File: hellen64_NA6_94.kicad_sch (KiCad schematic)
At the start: 208 parts, among them J1 USB_B_Mini, J11 Conn_01x01, J13 Conn_01x01, J14 Conn_01x01, J15 Conn_01x01, J16 Conn_01x01, J17 Conn_01x01, J19 Conn_01x01, J2 Conn_01x05_Male, J20 Conn_01x01, J21 Conn_01x01, J22 Conn_01x01, J24 Conn_01x01, J25 AudioJack3_SwitchTR, J27 Conn_01x06, J4 Conn_02x12_Odd_Even, J5 USB_B, M1 Module-input-0.1, M10 Module-power12-0.2, M11 Module-power5-0.2, M12 Module-wbo-0.3, M13 Module-can-0.1, M2 Module-ign8-0.2, M3 Module-mcu144-0.6, M4 Module-sd-0.1, M5 Module-output-0.3, M6 Module-dinput4-0.1, M7 Module-stlink-0.1, M8 Module-can-0.1, M9 Module-knock-0.1, P1 Pad, P10 Pad, P11 Pad, P12 Pad, P13 Pad, P14 Pad, P15 Pad, P16 Pad, P17 Pad, P18 Pad, P19 Pad, P2 178780-1, P20 Pad, P21 Pad, P22 Pad, P23 Pad, P24 Pad, P25 Pad, P26 Pad, P27 Pad, P28 Pad, P29 Pad, P3 Pad, P30 Pad, P31 Pad, P32 Pad, P33 Pad, P34 Pad, P35 Pad, P36 Pad, P37 Pad, P38 Pad, P39 Pad, P4 Pad, P40 Pad, P41 Pad, P42 Pad, P43 Pad, P44 Pad, P45 Pad, P46 Pad, P5 Pad, P6 Pad, P7 Pad, P8 Pad, P9 Pad, U1 LIS2DW12TR, U2 MPX4_MAP, U3 MCP6002-xSN, U4 LPS25HB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

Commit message: https://github.com/rusefi/hellenNA6_issues/issues/28
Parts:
- added U7: MPXH6400A, hellen-one-common:MPXH6400A-SSOP8, symbol MPX-4_MAP:MPX4_MAP
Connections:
- net +5VA: now also U7.2 (Vs)
- net GND: now also U7.3 (GND)
- net IN_MAP3: now also U7.4 (Vout)
- no-connect marks 59 -> 64
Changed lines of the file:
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@@
   (title_block
     (title "hellen64 NA6 94")
-    (date "2022-06-23")
+    (date "2022-06-24")
     (rev "С")
     (company "rusEFI")
@@
   (junction (at 26.67 392.43) (diameter 1.016) (color 0 0 0 0)
   )
+  (junction (at 265.43 228.6) (diameter 0) (color 0 0 0 0)
+  )
   (junction (at 62.23 43.18) (diameter 1.016) (color 0 0 0 0)
   )
@@
   (no_connect (at 365.76 165.1))
   (no_connect (at 518.16 377.19))
+  (no_connect (at 251.46 256.54))
   (no_connect (at 36.83 326.39))
   (no_connect (at 455.93 109.22))
@@
   (no_connect (at 307.34 50.8))
   (no_connect (at 36.83 311.15))
+  (no_connect (at 226.06 251.46))
   (no_connect (at 26.67 311.15))
   (no_connect (at 251.46 236.22))
@@
   (no_connect (at 69.85 38.1))
   (no_connect (at 307.34 53.34))
+  (no_connect (at 226.06 256.54))
   (no_connect (at 132.08 176.53))
+  (no_connect (at 226.06 254))
   (no_connect (at 415.29 114.3))
   (no_connect (at 307.34 45.72))
+  (no_connect (at 226.06 248.92))
   (no_connect (at 473.71 375.92))
   (no_connect (at 307.34 55.88))
@@
     (stroke (width 0) (type solid) (color 0 0 0 0))
   )
-  (wire (pts (xy 229.87 25.4) (xy 229.87 265.43))
+  (wire (pts (xy 229.87 25.4) (xy 229.87 243.84))
     (stroke (width 0) (type default) (color 0 0 0 0))
   )
@@
     (stroke (width 0) (type solid) (color 0 0 0 0))
   )
-  (wire (pts (xy 251.46 228.6) (xy 270.51 228.6))
+  (wire (pts (xy 251.46 228.6) (xy 265.43 228.6))
     (stroke (width 0) (type solid) (color 0 0 0 0))
   )
@@
     (stroke (width 0) (type solid) (color 0 0 0 0))
   )
+  (wire (pts (xy 265.43 228.6) (xy 270.51 228.6))
+    (stroke (width 0) (type solid) (color 0 0 0 0))
+  )
   (wire (pts (xy 111.76 233.68) (xy 220.98 233.68))
     (stroke (width 0) (type default) (color 0 0 0 0))
@@
     (stroke (width 0) (type solid) (color 0 0 0 0))
   )
+  (wire (pts (xy 259.08 254) (xy 251.46 254))
+    (stroke (width 0) (type default) (color 0 0 0 0))
+  )
   (bus (pts (xy 273.05 247.65) (xy 273.05 250.19))
     (stroke (width 0.3048) (type solid) (color 255 0 255 1))
@@
     (stroke (width 0) (type solid) (color 0 0 0 0))
   )
+  (wire (pts (xy 265.43 228.6) (xy 265.43 248.92))
+    (stroke (width 0) (type default) (color 0 0 0 0))
+  )
   (wire (pts (xy 39.37 353.06) (xy 36.83 353.06))
     (stroke (width 0) (type solid) (color 0 0 0 0))
@@
     (stroke (width 0) (type solid) (color 0 0 0 0))
   )
+  (wire (pts (xy 251.46 248.92) (xy 265.43 248.92))
+    (stroke (width 0) (type solid) (color 0 0 0 0))
+  )
   (wire (pts (xy 426.72 311.15) (xy 431.8 311.15))
     (stroke (width 0) (type default) (color 0 0 0 0))
@@
     (stroke (width 0) (type solid) (color 0 0 0 0))
   )
+  (wire (pts (xy 224.79 265.43) (xy 224.79 243.84))
+    (stroke (width 0) (type default) (color 0 0 0 0))
+  )
   (wire (pts (xy 46.99 358.14) (xy 59.69 358.14))
     (stroke (width 0) (type solid) (color 0 0 0 0))
@@
     (stroke (width 0) (type solid) (color 0 0 0 0))
   )
-  (wire (pts (xy 205.74 265.43) (xy 229.87 265.43))
+  (wire (pts (xy 205.74 265.43) (xy 224.79 265.43))
     (stroke (width 0) (type solid) (color 0 0 0 0))
   )
@@
     (stroke (width 0.3048) (type solid) (color 255 0 0 1))
   )
+  (wire (pts (xy 224.79 243.84) (xy 229.87 243.84))
+    (stroke (width 0) (type default) (color 0 0 0 0))
+  )
   (wire (pts (xy 271.78 212.09) (xy 309.88 212.09))
     (stroke (width 0) (type solid) (color 0 0 0 0))
@@
     (effects (font (size 1.27 1.27)) (justify right bottom))
   )
+  (label "IN_MAP3" (at 261.62 248.92 180)
+    (effects (font (size 1.27 1.27)) (justify right bottom))
+  )
   (label "IN_RES1" (at 297.18 240.03 0)
     (effects (font (size 1.27 1.27)) (justify left bottom))
@@
     (pin "1")
   )
+  (symbol (lib_id "power:+5VA") (at 259.08 254 270) (mirror x) (unit 1)
+    (in_bom yes) (on_board yes)
+    (property "Reference" "#PWR097" (id 0) (at 255.27 254 0)
+      (effects (font (size 1.27 1.27)) hide)
+    )
+    (property "Value" "+5VA" (id 1) (at 262.1344 253.6317 0))
+    (property "Footprint" "" (id 2) (at 259.08 254 0)
+      (effects (font (size 1.27 1.27)) hide)
+    )
+    (property "Datasheet" "" (id 3) (at 259.08 254 0)
+      (effects (font (size 1.27 1.27)) hide)
+    )
+    (pin "1")
+  )
   (symbol (lib_id "Device:C") (at 232.41 349.25 0) (mirror x) (unit 1)
     (in_bom yes) (on_board yes)
@@
     (pin "8")
   )
+  (symbol (lib_id "power:GND") (at 251.46 251.46 90) (mirror x) (unit 1)
+    (in_bom yes) (on_board yes)
+    (property "Reference" "#PWR055" (id 0) (at 257.81 251.46 0)
+      (effects (font (size 1.27 1.27)) hide)
+    )
+    (property "Value" "GND" (id 1) (at 255.905 251.46 90))
+    (property "Footprint" "" (id 2) (at 251.46 251.46 0)
+      (effects (font (size 1.27 1.27)) hide)
+    )
+    (property "Datasheet" "" (id 3) (at 251.46 251.46 0)
+      (effects (font (size 1.27 1.27)) hide)
+    )
+    (pin "1")
+  )
   (symbol (lib_id "power:GND") (at 193.04 328.93 0) (unit 1)
     (in_bom yes) (on_board yes)
@@
     (pin "1")
   )
+  (symbol (lib_name "MPX4_MAP_1") (lib_id "MPX-4_MAP:MPX4_MAP") (at 245.11 251.46 180) (unit 1)
+    (in_bom yes) (on_board yes)
+    (property "Reference" "U7" (id 0) (at 235.6185 244.1867 0)
+      (effects (font (size 1.524 1.524)) (justify left))
+    )
+    (property "Value" "MPXH6400A" (id 1) (at 246.38 246.38 0)
+      (effects (font (size 1.524 1.524)) (justify left))
+    )
+    (property "Footprint" "hellen-one-common:MPXH6400A-SSOP8" (id 2) (at 245.11 251.46 0)
+      (effects (font (size 1.27 1.27)) hide)
+    )
+    (property "Datasheet" "" (id 3) (at 245.11 251.46 0)
+      (effects (font (size 1.524 1.524)) hide)
+    )
+    (property "LCSC" "C511770" (id 4) (at 245.11 251.46 0)
+      (effects (font (size 1.27 1.27)) hide)
+    )
+    (pin "1")
+    (pin "2")
+    (pin "3")
+    (pin "4")
+    (pin "5")
+    (pin "6")
+    (pin "7")
+    (pin "8")
+  )
   (symbol (lib_id "power:GNDA") (at 351.79 394.97 90) (unit 1)
     (in_bom yes) (on_board yes)
@@
       (reference "#PWR054") (unit 1) (value "GNDA") (footprint "")
     )
+    (path "/6d0f4391-b1b5-4f82-a38f-c8996f5bd03b"
+      (reference "#PWR055") (unit 1) (value "GND") (footprint "")
+    )
     (path "/59a75caf-a40f-4cf5-b8bb-e65ae86bec15"
       (reference "#PWR056") (unit 1) (value "+5VAS") (footprint "")
@@
       (reference "#PWR096") (unit 1) (value "GND") (footprint "")
     )
+    (path "/0f0b90ed-ded0-4d03-90ce-6fee61ad0de8"
+      (reference "#PWR097") (unit 1) (value "+5VA") (footprint "")
+    )
     (path "/85f12dc3-c9a5-46a2-8a35-32f334558a91"
       (reference "#PWR098") (unit 1) (value "GNDA") (footprint "")
@@
       (reference "U6") (unit 1) (value "TLS115") (footprint "hellen-one-common:PG-DSO-8-43")
     )
+    (path "/b9979076-3600-40a5-8d36-93f7a5930242"
+      (reference "U7") (unit 1) (value "MPXH6400A") (footprint "hellen-one-common:MPXH6400A-SSOP8")
+    )
   )

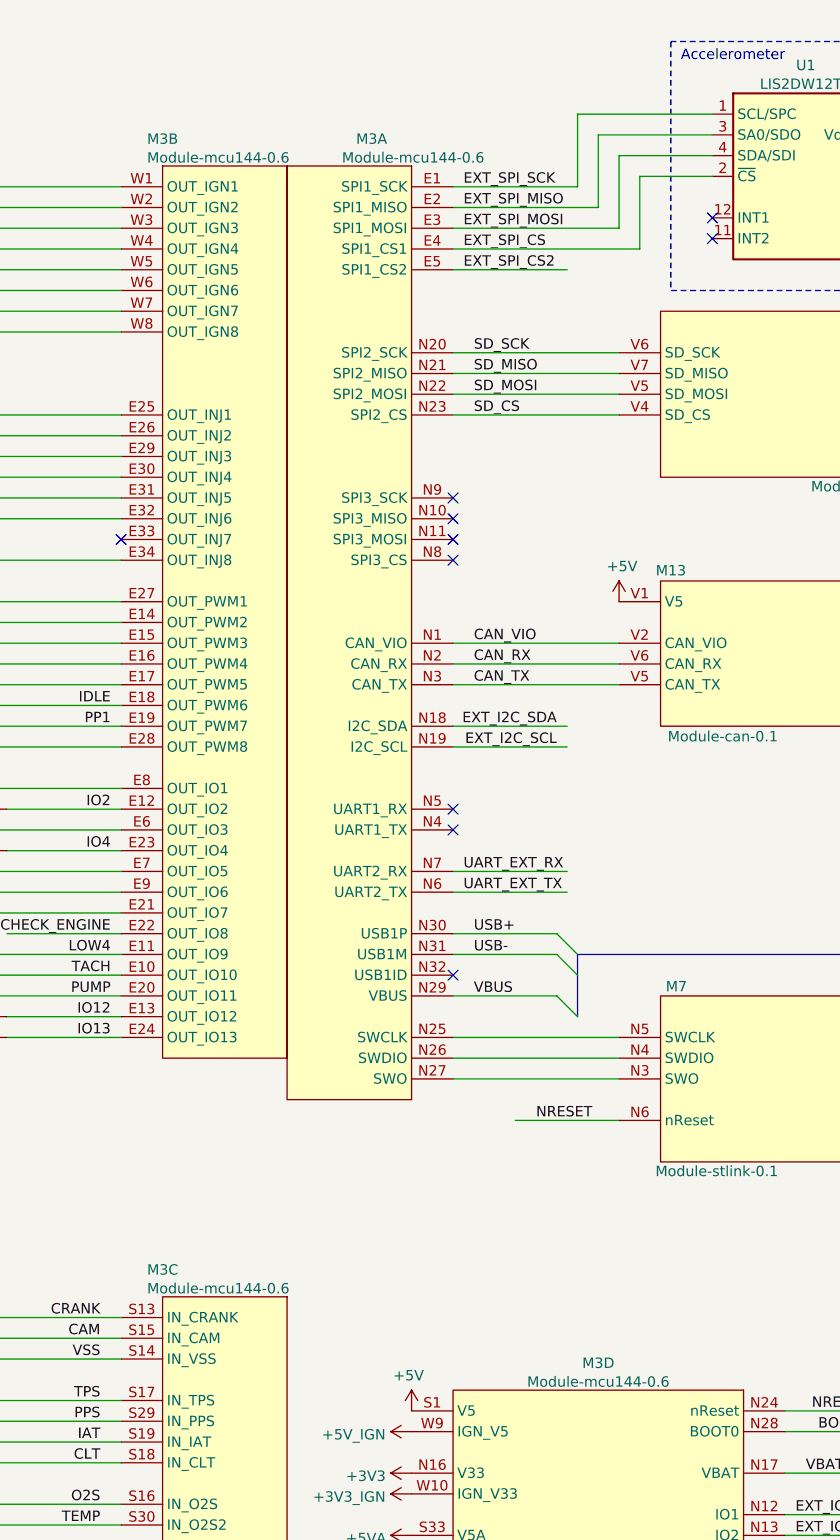
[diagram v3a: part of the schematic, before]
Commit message: mcu144 -> mcu
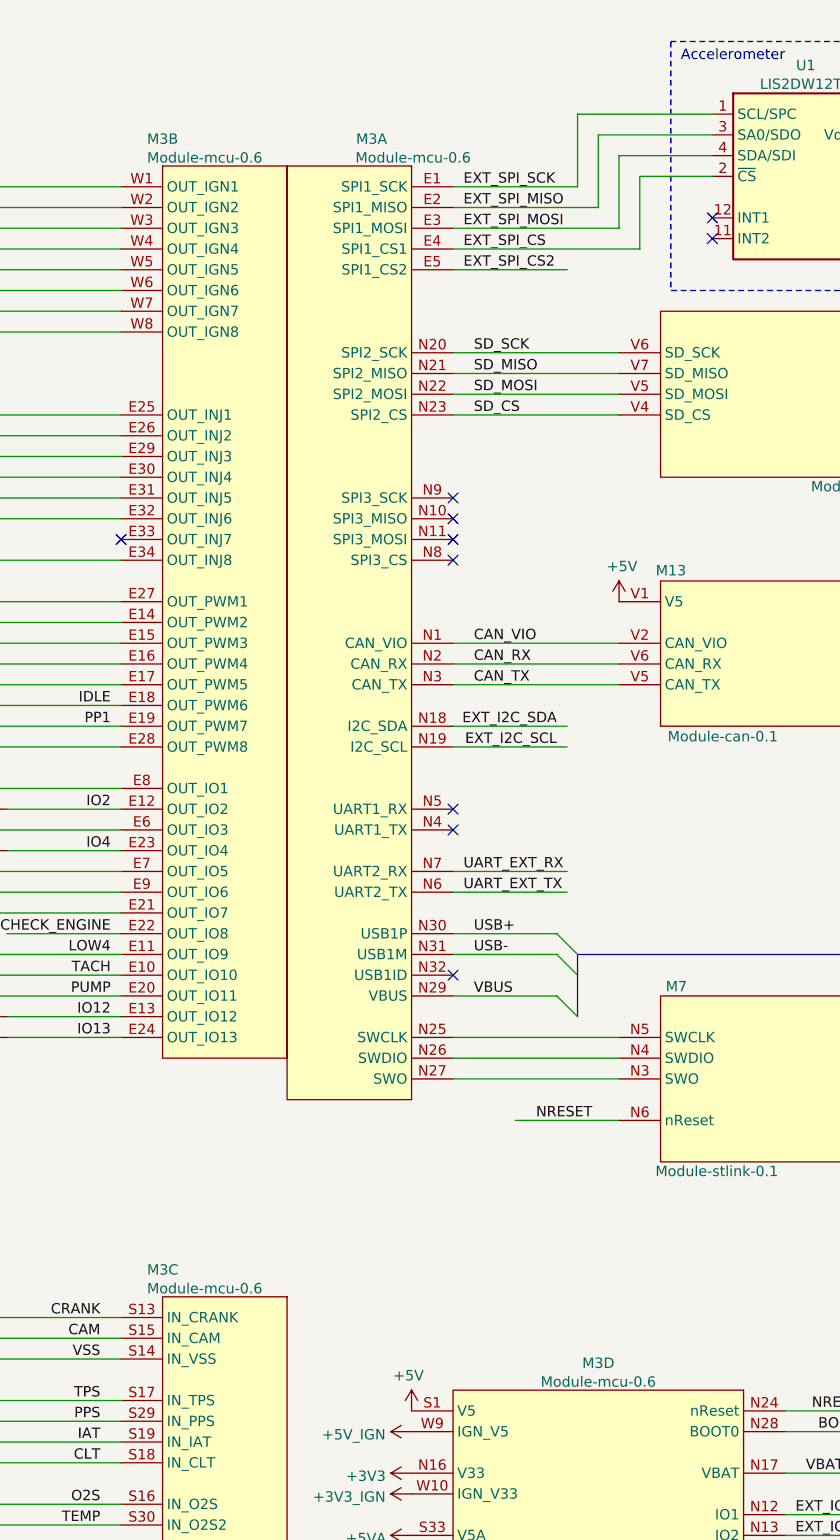
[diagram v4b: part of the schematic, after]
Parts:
- M3: value Module-mcu144-0.6 -> Module-mcu-0.6
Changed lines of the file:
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@@
   (title_block
     (title "hellen64 NA6 94")
-    (date "2022-06-24")
+    (date "2022-06-25")
     (rev "С")
     (company "rusEFI")
@@
       (effects (font (size 1.27 1.27)) (justify left))
     )
-    (property "Value" "Module-mcu144-0.6" (id 1) (at 418.4651 206.0078 0)
+    (property "Value" "Module-mcu-0.6" (id 1) (at 418.4651 206.0078 0)
       (effects (font (size 1.27 1.27)) (justify left))
     )
@@
       (effects (font (size 1.27 1.27)) (justify right))
     )
-    (property "Value" "Module-mcu144-0.6" (id 1) (at 418.4651 67.5778 0)
+    (property "Value" "Module-mcu-0.6" (id 1) (at 418.4651 67.5778 0)
       (effects (font (size 1.27 1.27)) (justify right))
     )
@@
     (in_bom yes) (on_board yes)
     (property "Reference" "M3" (id 0) (at 445.9605 65.2738 0))
-    (property "Value" "Module-mcu144-0.6" (id 1) (at 451.0405 67.5725 0))
+    (property "Value" "Module-mcu-0.6" (id 1) (at 451.0405 67.5725 0))
     (property "Footprint" "hellen-one-mcu-0.5:mcu" (id 2) (at 435.61 68.58 0)
       (effects (font (size 1.27 1.27)) hide)
@@
     (in_bom yes) (on_board yes) (fields_autoplaced)
     (property "Reference" "M3" (id 0) (at 473.71 215.1338 0))
-    (property "Value" "Module-mcu144-0.6" (id 1) (at 473.71 217.4325 0))
+    (property "Value" "Module-mcu-0.6" (id 1) (at 473.71 217.4325 0))
     (property "Footprint" "hellen-one-mcu-0.5:mcu" (id 2) (at 455.93 218.44 0)
       (effects (font (size 1.27 1.27)) hide)
@@
     )
     (path "/a6bf355d-1d5f-4e79-8e3f-45e3bddf3ceb"
-      (reference "M3") (unit 1) (value "Module-mcu144-0.6") (footprint "hellen-one-mcu-0.5:mcu")
+      (reference "M3") (unit 1) (value "Module-mcu-0.6") (footprint "hellen-one-mcu-0.5:mcu")
     )
     (path "/915d735b-9683-4d94-8b0d-1fa27ebac489"
-      (reference "M3") (unit 2) (value "Module-mcu144-0.6") (footprint "hellen-one-mcu-0.5:mcu")
+      (reference "M3") (unit 2) (value "Module-mcu-0.6") (footprint "hellen-one-mcu-0.5:mcu")
     )
     (path "/5f1c7f30-e456-4e5e-847b-c87579bb1a4c"
-      (reference "M3") (unit 3) (value "Module-mcu144-0.6") (footprint "hellen-one-mcu-0.5:mcu")
+      (reference "M3") (unit 3) (value "Module-mcu-0.6") (footprint "hellen-one-mcu-0.5:mcu")
     )
     (path "/a7d95f89-5755-415c-ab05-3cba0bcc1e6a"
-      (reference "M3") (unit 4) (value "Module-mcu144-0.6") (footprint "hellen-one-mcu-0.5:mcu")
+      (reference "M3") (unit 4) (value "Module-mcu-0.6") (footprint "hellen-one-mcu-0.5:mcu")
     )
     (path "/46c92d79-ab77-4cea-933a-f95fdcee2757"

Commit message: rev.D with mcu-144
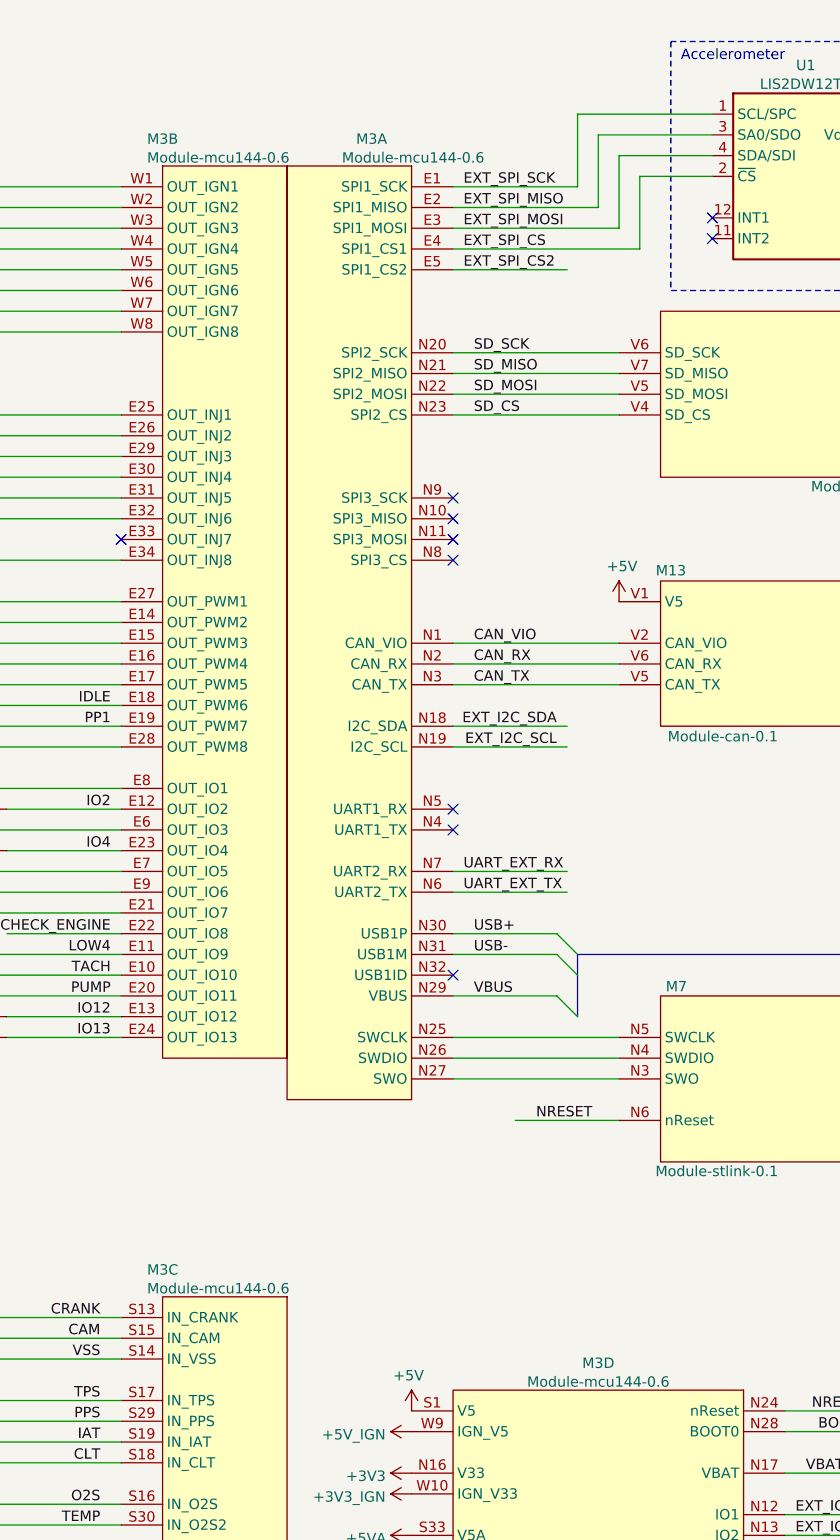
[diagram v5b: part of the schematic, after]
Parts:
- M3: value Module-mcu-0.6 -> Module-mcu144-0.6
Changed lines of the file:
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@@
   (title_block
     (title "hellen64 NA6 94")
-    (date "2022-06-25")
-    (rev "С")
+    (date "2022-08-24")
+    (rev "D")
     (company "rusEFI")
     (comment 7 "http://rusefi.com/s/hellenNA6")
@@
       (effects (font (size 1.27 1.27)) (justify left))
     )
-    (property "Value" "Module-mcu-0.6" (id 1) (at 418.4651 206.0078 0)
+    (property "Value" "Module-mcu144-0.6" (id 1) (at 418.4651 206.0078 0)
       (effects (font (size 1.27 1.27)) (justify left))
     )
@@
       (effects (font (size 1.27 1.27)) (justify right))
     )
-    (property "Value" "Module-mcu-0.6" (id 1) (at 418.4651 67.5778 0)
+    (property "Value" "Module-mcu144-0.6" (id 1) (at 418.4651 67.5778 0)
       (effects (font (size 1.27 1.27)) (justify right))
     )
@@
     (in_bom yes) (on_board yes)
     (property "Reference" "M3" (id 0) (at 445.9605 65.2738 0))
-    (property "Value" "Module-mcu-0.6" (id 1) (at 451.0405 67.5725 0))
+    (property "Value" "Module-mcu144-0.6" (id 1) (at 451.0405 67.5725 0))
     (property "Footprint" "hellen-one-mcu-0.5:mcu" (id 2) (at 435.61 68.58 0)
       (effects (font (size 1.27 1.27)) hide)
@@
     (in_bom yes) (on_board yes) (fields_autoplaced)
     (property "Reference" "M3" (id 0) (at 473.71 215.1338 0))
-    (property "Value" "Module-mcu-0.6" (id 1) (at 473.71 217.4325 0))
+    (property "Value" "Module-mcu144-0.6" (id 1) (at 473.71 217.4325 0))
     (property "Footprint" "hellen-one-mcu-0.5:mcu" (id 2) (at 455.93 218.44 0)
       (effects (font (size 1.27 1.27)) hide)
@@
     )
     (path "/a6bf355d-1d5f-4e79-8e3f-45e3bddf3ceb"
-      (reference "M3") (unit 1) (value "Module-mcu-0.6") (footprint "hellen-one-mcu-0.5:mcu")
+      (reference "M3") (unit 1) (value "Module-mcu144-0.6") (footprint "hellen-one-mcu-0.5:mcu")
     )
     (path "/915d735b-9683-4d94-8b0d-1fa27ebac489"
-      (reference "M3") (unit 2) (value "Module-mcu-0.6") (footprint "hellen-one-mcu-0.5:mcu")
+      (reference "M3") (unit 2) (value "Module-mcu144-0.6") (footprint "hellen-one-mcu-0.5:mcu")
     )
     (path "/5f1c7f30-e456-4e5e-847b-c87579bb1a4c"
-      (reference "M3") (unit 3) (value "Module-mcu-0.6") (footprint "hellen-one-mcu-0.5:mcu")
+      (reference "M3") (unit 3) (value "Module-mcu144-0.6") (footprint "hellen-one-mcu-0.5:mcu")
     )
     (path "/a7d95f89-5755-415c-ab05-3cba0bcc1e6a"
-      (reference "M3") (unit 4) (value "Module-mcu-0.6") (footprint "hellen-one-mcu-0.5:mcu")
+      (reference "M3") (unit 4) (value "Module-mcu144-0.6") (footprint "hellen-one-mcu-0.5:mcu")
     )
     (path "/46c92d79-ab77-4cea-933a-f95fdcee2757"
